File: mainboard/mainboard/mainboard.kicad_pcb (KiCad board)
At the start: 2 copper layers, 100 x 100 mm, 95 parts, among them IC501 SN74HCS138PWR, IC502 SN74HCS138PWR, IC503 SN74HCS138PWR, IC504 SN74HCS138PWR, IC505 SN74HCS151PWR, J201 Power LED connector, J202 Power button connector, J301 DC-005-5A-2.0, J601 Connector 1, J602 Connector 6, J603 Connector 5, J604 Connector 4, J605 Connector 1, J606 Connector 3, J607 Connector 2, J608 I2C 2, J609 Conn_01x03_Female, J610 Conn_01x03_Female, J611 I2C 1, J612 I2C 3, J801 Micro_SD_Card, U201 RP2040, U301 LD1117S50TR_SOT223, U303 BD9D321EFJ, U304 BD9D321EFJ, U401 W25Q128JVS, U701 hs8836a, Y201 ECS-120-8-36-CGN-TR

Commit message: motherboard designed
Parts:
- added TP301: TestPoint, TestPoint:TestPoint_Loop_D1.80mm_Drill1.0mm_Beaded, F.Cu at (45.0, 149.0)
- added TP302: TestPoint, TestPoint:TestPoint_Pad_D1.5mm, F.Cu at (47.0, 141.0)
- added TP303: TestPoint, TestPoint:TestPoint_Loop_D1.80mm_Drill1.0mm_Beaded, F.Cu at (120.0, 85.0)
- added TP304: TestPoint, TestPoint:TestPoint_Loop_D1.80mm_Drill1.0mm_Beaded, F.Cu at (103.0, 128.0)
- added TP305: TestPoint, TestPoint:TestPoint_Pad_D1.5mm, F.Cu at (120.4, 89.6)
- added TP306: TestPoint, TestPoint:TestPoint_Pad_D1.5mm, F.Cu at (99.0, 125.0)
- moved R801 1.20 mm to (70.2, 114.9)
- moved R802 1.13 mm to (70.2, 118.4)
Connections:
- net +3V3_BUS renamed +3V3
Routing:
- net /Connectors/BUS.D0: track 91.7 -> 173.7 mm
- net /Connectors/BUS.D1: track 92.6 -> 174.1 mm
- net /Connectors/BUS.SCLK: track 92.6 -> 174.1 mm
- net /Connectors/BUS.RWDS: track 92.2 -> 173.7 mm
- net /Connectors/BUS.D2: track 92.8 -> 142.0 mm
- net /Connectors/BUS.D3: track 93.0 -> 142.0 mm
- net /RP2040 Core/SDIO.D2: track 36.2 -> 55.4 mm
- net /RP2040 Core/SDIO.D3: track 37.0 -> 55.5 mm
- net /RP2040 Core/SDIO.CMD: track 38.2 -> 55.4 mm
- net /Connectors/BUS.D6: track 92.9 -> 108.7 mm
- net /Connectors/BUS.D7: track 93.0 -> 108.7 mm
- net /Connectors/BUS.D4: track 92.9 -> 108.6 mm
- net /Connectors/BUS.D5: track 93.1 -> 108.7 mm
- net /RP2040 Core/SDIO.D1: track 41.8 -> 55.5 mm
- net /Flash memory/FLASH.SD2: track 8.12 -> 20.2 mm
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
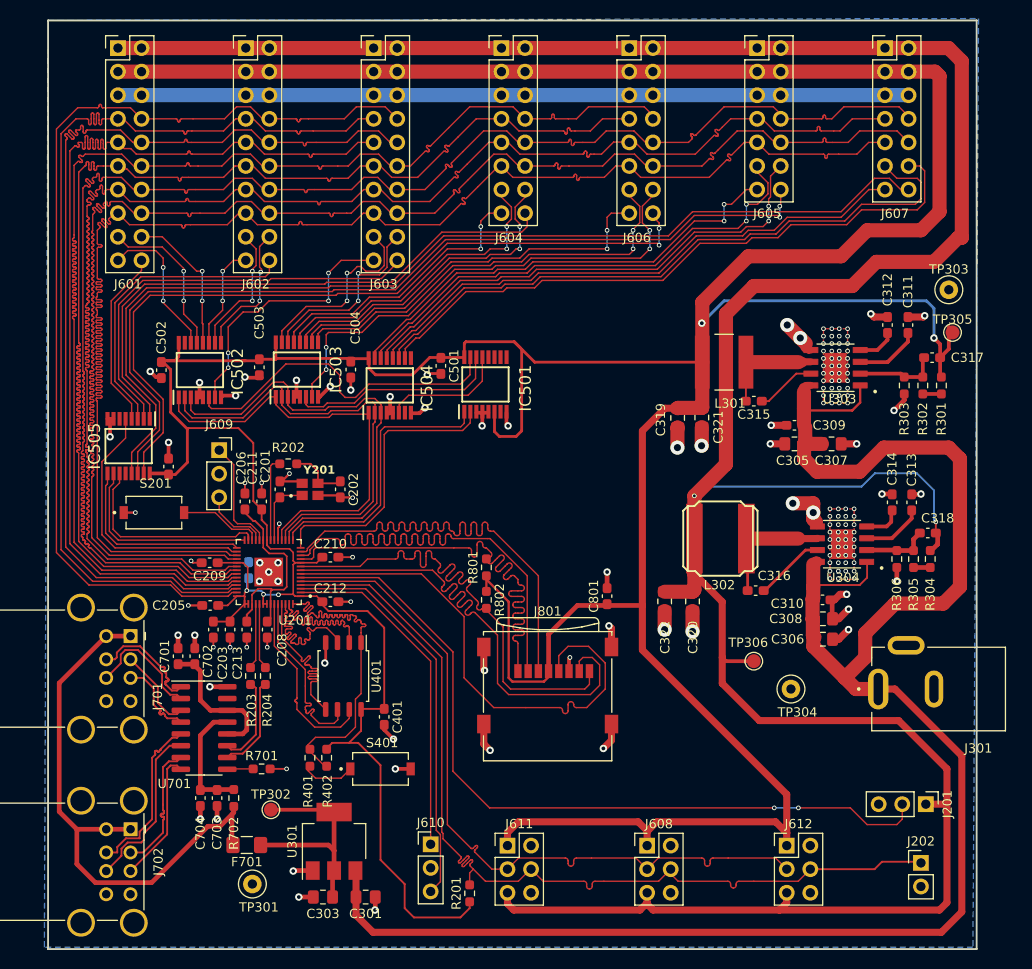
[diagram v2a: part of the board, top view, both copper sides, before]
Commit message: gpu and motherboard passes tests, now time for fpga
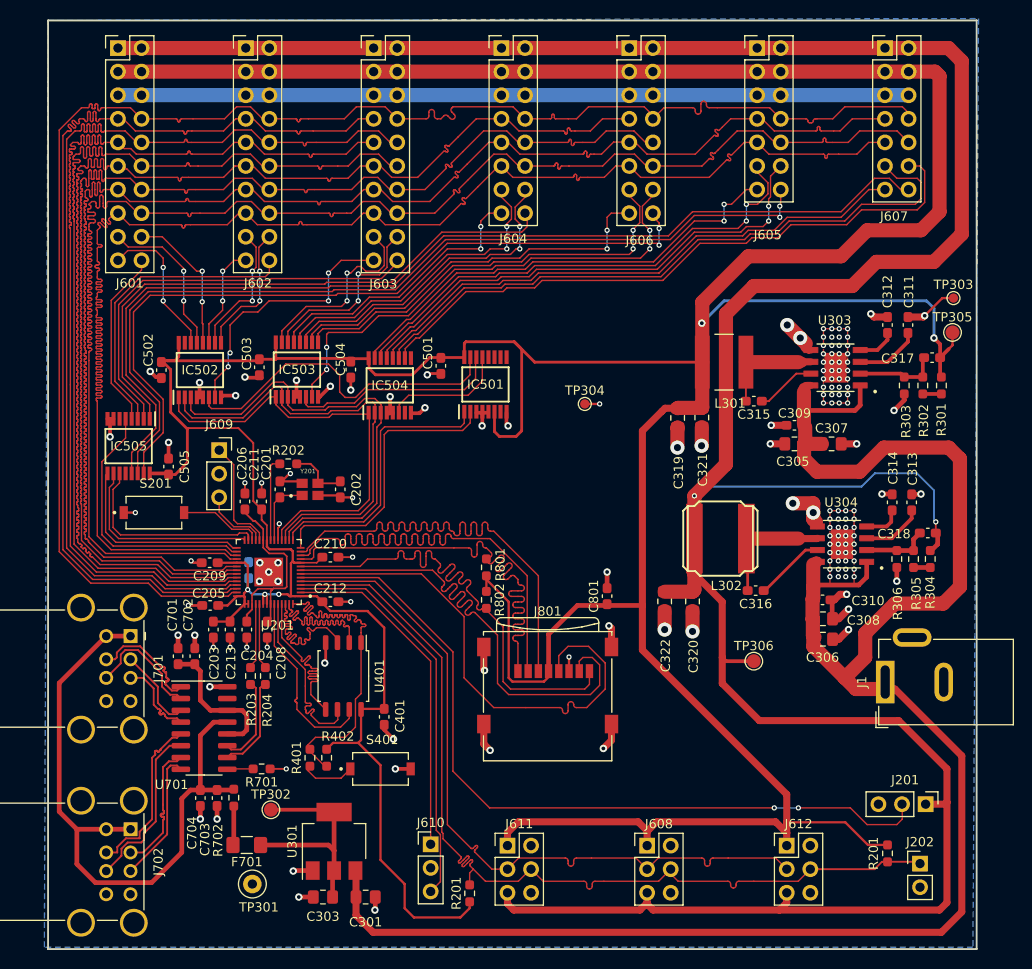
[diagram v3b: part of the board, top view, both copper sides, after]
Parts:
- removed J301: DC-005-5A-2.0, footprints:XKB_DC-005-5A-2.0
- added J1: Barrel_Jack_Switch, Connector_BarrelJack:BarrelJack_GCT_DCJ200-10-A_Horizontal, F.Cu at (113.2, 127.2)
- added R201: 10k, Resistor_SMD:R_0603_1608Metric_Pad0.98x0.95mm_HandSolder, F.Cu at (113.4, 145.7)
- TP303, TP304: footprint TestPoint:TestPoint_Loop_D1.80mm_Drill1.0mm_Beaded -> TestPoint:TestPoint_Pad_D1.0mm
- moved TP304 37.9 mm to (80.8, 97.3)
- moved TP303 1.03 mm to (120.5, 85.9)
- moved J202 0.13 mm to (116.9, 146.8)
- turned R702 to 90 degrees
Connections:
- net /Bus multiplexers & demultiplexers/BUS.CS0 renamed /Bus multiplexers & demultiplexers/BUS_CS0
- net /Bus multiplexers & demultiplexers/BUS.CS1 renamed /Bus multiplexers & demultiplexers/BUS_CS1
- net /Bus multiplexers & demultiplexers/BUS.CS10 renamed /Bus multiplexers & demultiplexers/BUS_CS10
- net /Bus multiplexers & demultiplexers/BUS.CS11 renamed /Bus multiplexers & demultiplexers/BUS_CS11
- net /Bus multiplexers & demultiplexers/BUS.CS12 renamed /Bus multiplexers & demultiplexers/BUS_CS12
- net /Bus multiplexers & demultiplexers/BUS.CS13 renamed /Bus multiplexers & demultiplexers/BUS_CS13
- net /Bus multiplexers & demultiplexers/BUS.CS2 renamed /Bus multiplexers & demultiplexers/BUS_CS2
- net /Bus multiplexers & demultiplexers/BUS.CS3 renamed /Bus multiplexers & demultiplexers/BUS_CS3
- net /Bus multiplexers & demultiplexers/BUS.CS4 renamed /Bus multiplexers & demultiplexers/BUS_CS4
- net /Bus multiplexers & demultiplexers/BUS.CS5 renamed /Bus multiplexers & demultiplexers/BUS_CS5
- net /Bus multiplexers & demultiplexers/BUS.CS6 renamed /Bus multiplexers & demultiplexers/BUS_CS6
- net /Bus multiplexers & demultiplexers/BUS.CS7 renamed /Bus multiplexers & demultiplexers/BUS_CS7
- net /Bus multiplexers & demultiplexers/BUS.CS8 renamed /Bus multiplexers & demultiplexers/BUS_CS8
- net /Bus multiplexers & demultiplexers/BUS.CS9 renamed /Bus multiplexers & demultiplexers/BUS_CS9
- net /Bus multiplexers & demultiplexers/BUS.CTRL0 renamed /Bus multiplexers & demultiplexers/BUS_CTRL0
- net /Bus multiplexers & demultiplexers/BUS.CTRL1 renamed /Bus multiplexers & demultiplexers/BUS_CTRL1
- net /Bus multiplexers & demultiplexers/BUS.CTRL2 renamed /Bus multiplexers & demultiplexers/BUS_CTRL2
- net /Bus multiplexers & demultiplexers/BUS.CTRL3 renamed /Bus multiplexers & demultiplexers/BUS_CTRL3
- net /Bus multiplexers & demultiplexers/BUS.CTRL4 renamed /Bus multiplexers & demultiplexers/BUS_CTRL4
- net /Bus multiplexers & demultiplexers/BUS.INT0 renamed /Bus multiplexers & demultiplexers/BUS_INT0
- net /Bus multiplexers & demultiplexers/BUS.INT1 renamed /Bus multiplexers & demultiplexers/BUS_INT1
- net /Bus multiplexers & demultiplexers/BUS.INT2 renamed /Bus multiplexers & demultiplexers/BUS_INT2
- net /Bus multiplexers & demultiplexers/BUS.INT3 renamed /Bus multiplexers & demultiplexers/BUS_INT3
- net /Bus multiplexers & demultiplexers/BUS.INT4 renamed /Bus multiplexers & demultiplexers/BUS_INT4
- net /Bus multiplexers & demultiplexers/BUS.INT5 renamed /Bus multiplexers & demultiplexers/BUS_INT5
- net /Bus multiplexers & demultiplexers/BUS.INT6 renamed /Bus multiplexers & demultiplexers/BUS_INT6
- net /Bus multiplexers & demultiplexers/BUS.RE0 renamed /Bus multiplexers & demultiplexers/BUS_RE0
- net /Bus multiplexers & demultiplexers/BUS.RE1 renamed /Bus multiplexers & demultiplexers/BUS_RE1
- net /Bus multiplexers & demultiplexers/BUS.RE2 renamed /Bus multiplexers & demultiplexers/BUS_RE2
- net /Bus multiplexers & demultiplexers/BUS.RE3 renamed /Bus multiplexers & demultiplexers/BUS_RE3
- net /Bus multiplexers & demultiplexers/BUS.RE4 renamed /Bus multiplexers & demultiplexers/BUS_RE4
- net /Bus multiplexers & demultiplexers/BUS.RE5 renamed /Bus multiplexers & demultiplexers/BUS_RE5
- net /Bus multiplexers & demultiplexers/BUS.RE6 renamed /Bus multiplexers & demultiplexers/BUS_RE6
- net DEMUX_1_EN renamed /Bus multiplexers & demultiplexers/DEMUX_1_EN
- net DEMUX_2_EN renamed /Bus multiplexers & demultiplexers/DEMUX_2_EN
- net DEMUX_3_EN renamed /Bus multiplexers & demultiplexers/DEMUX_3_EN
- net OSC_XIN renamed /RP2040 Core/OSC_IN
- net OSC_XOUT renamed /RP2040 Core/OSC_OUT
- net POWER_LED renamed /Connectors/POWER_LED
- C703 pad 1: Net-(U701-VCC) -> +5V_USB_HUB
- C704 pad 1: Net-(U701-VCC) -> +5V_USB_HUB
- F701 pad 2: +5V_USB_HUB -> Net-(F701-Pad2)
- IC501 pad 12: /Bus multiplexers & demultiplexers/BUS.RE_USB -> unconnected-(IC501-Y3)
- IC504 pad 7: /Bus multiplexers & demultiplexers/BUS.RE7 -> unconnected-(IC504-Y7)
- IC504 pad 9: /Bus multiplexers & demultiplexers/BUS.CS14 -> unconnected-(IC504-Y6)
- IC505 pad 12: /Bus multiplexers & demultiplexers/BUS.INT7 -> unconnected-(IC505-D7)
- J601 pad 10: /Connectors/BUS.D5 -> /Connectors/BUS.D6
- J601 pad 11: /Connectors/BUS.D2 -> /Connectors/BUS.D3
- J601 pad 12: /Connectors/BUS.D3 -> /Connectors/BUS.D4
- J601 pad 13: /Connectors/BUS.D0 -> /Connectors/BUS.D1
- J601 pad 14: /Connectors/BUS.D1 -> /Connectors/BUS.D2
- J601 pad 16: /Connectors/BUS.RWDS -> /Connectors/BUS.D0
- J601 pad 7: /Connectors/BUS.D6 -> /Connectors/BUS.D7
- J601 pad 8: /Connectors/BUS.D7 -> /Connectors/BUS.RWDS
- J601 pad 9: /Connectors/BUS.D4 -> /Connectors/BUS.D5
- J602 pad 10: /Connectors/BUS.D5 -> /Connectors/BUS.D6
- J602 pad 11: /Connectors/BUS.D2 -> /Connectors/BUS.D3
- J602 pad 12: /Connectors/BUS.D3 -> /Connectors/BUS.D4
- J602 pad 13: /Connectors/BUS.D0 -> /Connectors/BUS.D1
- J602 pad 14: /Connectors/BUS.D1 -> /Connectors/BUS.D2
- J602 pad 16: /Connectors/BUS.RWDS -> /Connectors/BUS.D0
- J602 pad 7: /Connectors/BUS.D6 -> /Connectors/BUS.D7
- J602 pad 8: /Connectors/BUS.D7 -> /Connectors/BUS.RWDS
- J602 pad 9: /Connectors/BUS.D4 -> /Connectors/BUS.D5
- J603 pad 10: /Connectors/BUS.D5 -> /Connectors/BUS.D6
- J603 pad 11: /Connectors/BUS.D2 -> /Connectors/BUS.D3
- J603 pad 12: /Connectors/BUS.D3 -> /Connectors/BUS.D4
- J603 pad 13: /Connectors/BUS.D0 -> /Connectors/BUS.D1
- J603 pad 14: /Connectors/BUS.D1 -> /Connectors/BUS.D2
- J603 pad 16: /Connectors/BUS.RWDS -> /Connectors/BUS.D0
- J603 pad 7: /Connectors/BUS.D6 -> /Connectors/BUS.D7
- J603 pad 8: /Connectors/BUS.D7 -> /Connectors/BUS.RWDS
- J603 pad 9: /Connectors/BUS.D4 -> /Connectors/BUS.D5
- J604 pad 10: /Connectors/BUS.D1 -> /Connectors/BUS.D2
- J604 pad 12: /Connectors/BUS.RWDS -> /Connectors/BUS.D0
- J604 pad 7: /Connectors/BUS.D2 -> /Connectors/BUS.D3
- J604 pad 8: /Connectors/BUS.D3 -> /Connectors/BUS.RWDS
- J604 pad 9: /Connectors/BUS.D0 -> /Connectors/BUS.D1
- J605 pad 10: /Connectors/BUS.RWDS -> /Connectors/BUS.D0
- J605 pad 7: /Connectors/BUS.D0 -> /Connectors/BUS.D1
- J605 pad 8: /Connectors/BUS.D1 -> /Connectors/BUS.RWDS
- J606 pad 10: /Connectors/BUS.D1 -> /Connectors/BUS.D2
- J606 pad 12: /Connectors/BUS.RWDS -> /Connectors/BUS.D0
- J606 pad 7: /Connectors/BUS.D2 -> /Connectors/BUS.D3
- J606 pad 8: /Connectors/BUS.D3 -> /Connectors/BUS.RWDS
- J606 pad 9: /Connectors/BUS.D0 -> /Connectors/BUS.D1
- J607 pad 10: /Connectors/BUS.RWDS -> /Connectors/BUS.D0
- J607 pad 7: /Connectors/BUS.D0 -> /Connectors/BUS.D1
- J607 pad 8: /Connectors/BUS.D1 -> /Connectors/BUS.RWDS
- R702 pad 1: Net-(U701-VCC) -> Net-(F701-Pad2)
- TP304 pad 1: (no net) -> GND
- U201 pad 32: /Connectors/BUS.RWDS -> /Connectors/BUS.D0
- U201 pad 34: /Connectors/BUS.D0 -> /Connectors/BUS.D1
- U201 pad 35: /Connectors/BUS.D1 -> /Connectors/BUS.D2
- U201 pad 36: /Connectors/BUS.D2 -> /Connectors/BUS.D3
- U201 pad 37: /Connectors/BUS.D3 -> /Connectors/BUS.D4
- U201 pad 38: /Connectors/BUS.D4 -> /Connectors/BUS.D5
- U201 pad 39: /Connectors/BUS.D5 -> /Connectors/BUS.D6
- U201 pad 40: /Connectors/BUS.D6 -> /Connectors/BUS.D7
- U201 pad 41: /Connectors/BUS.D7 -> /Connectors/BUS.RWDS
- U701 pad 13: Net-(U701-VCC) -> +5V_USB_HUB
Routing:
- net Net-(U701-VCC): track 13.0 -> 0.00 mm
- net +3V3: track 526.9 -> 539.0 mm
- net +5V_USB_HUB: track 60.9 -> 70.5 mm
- net GND: track 216.8 -> 223.8 mm, vias 155 -> 148
- net Net-(F701-Pad2): track 0.00 -> 4.22 mm
- net /Connectors/BUS.RWDS: track 173.7 -> 175.8 mm
- net /Connectors/BUS.D6: track 108.7 -> 109.9 mm
- net /Connectors/BUS.D0: track 173.7 -> 174.9 mm
- net /Connectors/BUS.SCLK: track 174.1 -> 174.9 mm
- net /Connectors/BUS.D4: track 108.6 -> 109.3 mm
- net /Connectors/BUS.D1: track 174.1 -> 174.9 mm
- net /Connectors/BUS.D7: track 108.7 -> 109.3 mm
- net /Connectors/BUS.D5: track 108.7 -> 109.2 mm
- net /Connectors/BUS.D2: track 142.0 -> 142.5 mm
- net /Connectors/BUS.D3: track 142.0 -> 142.5 mm

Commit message: refactored mainboard schematic
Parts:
- IC501: value SN74HCS138PWR -> SN74HCS238PWR
- moved J604 1.22 mm to (71.9, 60.2)
- moved J605 1.22 mm to (99.5, 60.2)
- moved J606 1.22 mm to (85.7, 60.2)
- moved J607 1.22 mm to (113.2, 60.2)
- moved J601 1.22 mm to (30.6, 60.2)
- moved J602 1.22 mm to (44.4, 60.2)
- moved J603 1.22 mm to (58.2, 60.2)
- moved IC501 0.10 mm to (70.1, 95.3)
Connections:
- J601 pad 2: +5V_BUS -> VDC
- J602 pad 2: +5V_BUS -> VDC
- J603 pad 2: +5V_BUS -> VDC
- J604 pad 2: +5V_BUS -> VDC
- J605 pad 2: +5V_BUS -> VDC
- J606 pad 2: +5V_BUS -> VDC
- J607 pad 2: +5V_BUS -> VDC
- J608 pad 2: unconnected-(J608-Pin_2) -> VDC
- J611 pad 2: unconnected-(J611-Pin_2) -> VDC
- J612 pad 2: unconnected-(J612-Pin_2) -> VDC
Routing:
- net VDC: track 196.5 -> 393.8 mm, vias 0 -> 4
- net +5V_BUS: track 322.6 -> 345.1 mm
- net /Bus multiplexers & demultiplexers/BUS_CS4: track 28.6 -> 26.2 mm
- net /Bus multiplexers & demultiplexers/BUS_RE2: track 20.3 -> 18.4 mm
- net /Bus multiplexers & demultiplexers/BUS_CS3: track 14.5 -> 12.7 mm
- net /Connectors/BUS.D3: track 142.5 -> 144.3 mm
- net /Bus multiplexers & demultiplexers/BUS_RE1: track 14.6 -> 12.9 mm
- net /Bus multiplexers & demultiplexers/BUS_INT3: track 62.0 -> 60.4 mm
- net /Bus multiplexers & demultiplexers/BUS_INT2: track 45.6 -> 44.0 mm
- net /Bus multiplexers & demultiplexers/BUS_INT1: track 32.8 -> 31.2 mm
- net /Connectors/BUS.D1: track 174.9 -> 176.4 mm
- net /Connectors/BUS.D4: track 109.3 -> 110.8 mm
- net /Connectors/BUS.D5: track 109.2 -> 110.7 mm
- net /Bus multiplexers & demultiplexers/BUS_INT6: track 110.8 -> 109.4 mm
- net +3V3: track 539.0 -> 537.6 mm
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
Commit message: working on new pcb
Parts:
- removed C201, C202: 14p, Capacitor_SMD:C_0603_1608Metric_Pad1.08x0.95mm_HandSolder
- removed C204, C311, C313: 1u, Capacitor_SMD:C_0603_1608Metric_Pad1.08x0.95mm_HandSolder
- removed C206, C208, C209, C210, C211, C212, C213, C309, C310, C315, C316, C401, C501, C502, C503, C504, C505, C702, C704: 100n, Capacitor_SMD:C_0603_1608Metric_Pad1.08x0.95mm_HandSolder
- removed C301: 4.7u, Capacitor_SMD:C_0805_2012Metric_Pad1.18x1.45mm_HandSolder
- removed C303: 10uF, Capacitor_SMD:C_0805_2012Metric_Pad1.18x1.45mm_HandSolder
- removed C305, C306, C307, C308: 10u, Capacitor_SMD:C_0805_2012Metric_Pad1.18x1.45mm_HandSolder
- removed C312, C314: 3300p, Capacitor_SMD:C_0603_1608Metric_Pad1.08x0.95mm_HandSolder
- removed C317, C318: 22p, Capacitor_SMD:C_0603_1608Metric_Pad1.08x0.95mm_HandSolder
- removed C319, C320, C321, C322: 22u, Capacitor_SMD:C_0805_2012Metric_Pad1.18x1.45mm_HandSolder
- removed C701, C703: 4.7u, Capacitor_SMD:C_0603_1608Metric_Pad1.08x0.95mm_HandSolder
- removed C801: 10u, Capacitor_SMD:C_0603_1608Metric_Pad1.08x0.95mm_HandSolder
- removed F701: 500mA, Fuse:Fuse_1206_3216Metric_Pad1.42x1.75mm_HandSolder
- removed IC501: SN74HCS238PWR, footprints:SOP65P640X120-16N
- removed IC502, IC503, IC504: SN74HCS138PWR, footprints:SOP65P640X120-16N
- removed IC505: SN74HCS151PWR, footprints:SOP65P640X120-16N
- removed J201: Power LED connector, Connector_PinHeader_2.54mm:PinHeader_1x03_P2.54mm_Vertical
- removed J202: Power button connector, Connector_PinHeader_2.54mm:PinHeader_1x02_P2.54mm_Vertical
- removed J601: Connector 1, Connector_PinHeader_2.54mm:PinHeader_2x10_P2.54mm_Vertical
- removed J602: Connector 6, Connector_PinHeader_2.54mm:PinHeader_2x10_P2.54mm_Vertical
- removed J603: Connector 5, Connector_PinHeader_2.54mm:PinHeader_2x10_P2.54mm_Vertical
- removed J604: Connector 4, Connector_PinHeader_2.54mm:PinHeader_2x08_P2.54mm_Vertical
- removed J605: Connector 1, Connector_PinHeader_2.54mm:PinHeader_2x07_P2.54mm_Vertical
- removed J606: Connector 3, Connector_PinHeader_2.54mm:PinHeader_2x08_P2.54mm_Vertical
- removed J607: Connector 2, Connector_PinHeader_2.54mm:PinHeader_2x07_P2.54mm_Vertical
- removed J608: I2C 2, Connector_PinHeader_2.54mm:PinHeader_2x03_P2.54mm_Vertical
- removed J609: Conn_01x03_Female, Connector_PinSocket_2.54mm:PinSocket_1x03_P2.54mm_Vertical
- removed J610: Conn_01x03_Female, Connector_PinHeader_2.54mm:PinHeader_1x03_P2.54mm_Vertical
- removed J611: I2C 1, Connector_PinHeader_2.54mm:PinHeader_2x03_P2.54mm_Vertical
- removed J612: I2C 3, Connector_PinHeader_2.54mm:PinHeader_2x03_P2.54mm_Vertical
- removed J701, J702: ~, Connector_USB:USB_A_Wuerth_61400826021_Horizontal_Stacked
- removed J801: Micro_SD_Card, Connector_Card:microSD_HC_Wuerth_693072010801
- removed L301: 2.2u, footprints:IND_NR6028T4R7M
- removed L302: 3.3u, footprints:NRS8030
- removed R201 (x2), R402, R801, R802: 10k, Resistor_SMD:R_0603_1608Metric_Pad0.98x0.95mm_HandSolder
- removed R202, R401: 1k, Resistor_SMD:R_0603_1608Metric_Pad0.98x0.95mm_HandSolder
- removed R203, R204: 27.4R, Resistor_SMD:R_0603_1608Metric_Pad0.98x0.95mm_HandSolder
- removed R301: 68k, Resistor_SMD:R_0603_1608Metric_Pad0.98x0.95mm_HandSolder
- removed R302: 5.6k, Resistor_SMD:R_0603_1608Metric_Pad0.98x0.95mm_HandSolder
- removed R303, R306: 22k, Resistor_SMD:R_0603_1608Metric_Pad0.98x0.95mm_HandSolder
- removed R304: 120k, Resistor_SMD:R_0603_1608Metric_Pad0.98x0.95mm_HandSolder
- removed R305: 3.3k, Resistor_SMD:R_0603_1608Metric_Pad0.98x0.95mm_HandSolder
- removed R701: 100k, Resistor_SMD:R_0603_1608Metric_Pad0.98x0.95mm_HandSolder
- removed R702: 4.7, Resistor_SMD:R_0603_1608Metric_Pad0.98x0.95mm_HandSolder
- removed S201, S401: PTS636_SM43J_SMTR_LFS, footprints:SW_PTS636_SM43J_SMTR_LFS
- removed TP301: TestPoint, TestPoint:TestPoint_Loop_D1.80mm_Drill1.0mm_Beaded
- removed TP302, TP305, TP306: TestPoint, TestPoint:TestPoint_Pad_D1.5mm
- removed TP303, TP304: TestPoint, TestPoint:TestPoint_Pad_D1.0mm
- removed U201: RP2040, footprints:QFN40P700X700X90-57N
- removed U301: LD1117S50TR_SOT223, Package_TO_SOT_SMD:SOT-223-3_TabPin2
- removed U303, U304: BD9D321EFJ, footprints:SOIC127P600X100-9N
- removed U401: W25Q128JVS, Package_SO:SOIC-8_5.23x5.23mm_P1.27mm
- removed U701: hs8836a, Package_SO:SOP-16_3.9x9.9mm_P1.27mm
- removed Y201: ECS-120-8-36-CGN-TR, footprints:XTAL_ECS-120-8-36-CGN-TR
- added C1: 14p, Capacitor_SMD:C_0402_1005Metric_Pad0.74x0.62mm_HandSolder, F.Cu at (65.2, 57.8)
- added C10: 100n, Capacitor_SMD:C_0402_1005Metric_Pad0.74x0.62mm_HandSolder, F.Cu at (68.7, 63.8)
- added C11: 100n, Capacitor_SMD:C_0402_1005Metric_Pad0.74x0.62mm_HandSolder, F.Cu at (66.7, 69.1)
- added C12: 100n, Capacitor_SMD:C_0402_1005Metric_Pad0.74x0.62mm_HandSolder, F.Cu at (62.1, 71.9)
- added C13: 100n, Capacitor_SMD:C_0402_1005Metric_Pad0.74x0.62mm_HandSolder, F.Cu at (56.3, 69.2)
- added C14: 100n, Capacitor_SMD:C_0402_1005Metric_Pad0.74x0.62mm_HandSolder, F.Cu at (61.0, 71.2)
- added C15: 1u, Capacitor_SMD:C_0402_1005Metric_Pad0.74x0.62mm_HandSolder, F.Cu at (245.2, 61.9)
- added C16: 1u, Capacitor_SMD:C_0402_1005Metric_Pad0.74x0.62mm_HandSolder, F.Cu at (254.8, 63.9)
- added C17: 4.7u, Capacitor_SMD:C_0402_1005Metric_Pad0.74x0.62mm_HandSolder, F.Cu at (245.2, 60.0)
- added C18: 100pF, Capacitor_SMD:C_0402_1005Metric_Pad0.74x0.62mm_HandSolder, F.Cu at (245.2, 65.9)
- added C19: 100pF, Capacitor_SMD:C_0402_1005Metric_Pad0.74x0.62mm_HandSolder, F.Cu at (254.8, 65.9)
- added C2: 14p, Capacitor_SMD:C_0402_1005Metric_Pad0.74x0.62mm_HandSolder, F.Cu at (62.3, 54.4)
- added C20: 10uF, Capacitor_SMD:C_0402_1005Metric_Pad0.74x0.62mm_HandSolder, F.Cu at (245.2, 63.9)
- added C21: 2.2u, Capacitor_SMD:C_0402_1005Metric_Pad0.74x0.62mm_HandSolder, F.Cu at (254.8, 61.9)
- added C22: 2.2u, Capacitor_SMD:C_0402_1005Metric_Pad0.74x0.62mm_HandSolder, F.Cu at (254.8, 67.9)
- added C23: 10u, Capacitor_SMD:C_1206_3216Metric_Pad1.33x1.80mm_HandSolder, F.Cu at (134.1, 108.7)
- added C24: 10u, Capacitor_SMD:C_1206_3216Metric_Pad1.33x1.80mm_HandSolder, F.Cu at (117.0, 108.5)
- added C25: 10u, Capacitor_SMD:C_1206_3216Metric_Pad1.33x1.80mm_HandSolder, F.Cu at (131.4, 108.7)
- added C26: 10u, Capacitor_SMD:C_1206_3216Metric_Pad1.33x1.80mm_HandSolder, F.Cu at (114.3, 108.5)
- added C27: 100n, Capacitor_SMD:C_0402_1005Metric_Pad0.74x0.62mm_HandSolder, F.Cu at (136.0, 108.1)
- added C28: 100n, Capacitor_SMD:C_0402_1005Metric_Pad0.74x0.62mm_HandSolder, F.Cu at (118.9, 107.8)
- added C29: 1u, Capacitor_SMD:C_0402_1005Metric_Pad0.74x0.62mm_HandSolder, F.Cu at (144.3, 115.3)
- added C3: 1u, Capacitor_SMD:C_0402_1005Metric_Pad0.74x0.62mm_HandSolder, F.Cu at (58.7, 71.2)
- added C30: 3300p, Capacitor_SMD:C_0402_1005Metric_Pad0.74x0.62mm_HandSolder, F.Cu at (144.3, 114.2)
- added C31: 1u, Capacitor_SMD:C_0402_1005Metric_Pad0.74x0.62mm_HandSolder, F.Cu at (126.9, 115.2)
- added C32: 3300p, Capacitor_SMD:C_0402_1005Metric_Pad0.74x0.62mm_HandSolder, F.Cu at (126.9, 114.1)
- added C33: 100n, Capacitor_SMD:C_0402_1005Metric_Pad0.74x0.62mm_HandSolder, F.Cu at (135.0, 101.9)
- added C34: 100n, Capacitor_SMD:C_0402_1005Metric_Pad0.74x0.62mm_HandSolder, F.Cu at (119.5, 102.5)
- added C35: 22p, Capacitor_SMD:C_0402_1005Metric_Pad0.74x0.62mm_HandSolder, F.Cu at (140.3, 116.5)
- added C36: 22p, Capacitor_SMD:C_0402_1005Metric_Pad0.74x0.62mm_HandSolder, F.Cu at (123.2, 116.3)
- added C37: 22u, Capacitor_SMD:C_1206_3216Metric_Pad1.33x1.80mm_HandSolder, F.Cu at (144.7, 93.6)
- added C38: 22u, Capacitor_SMD:C_1206_3216Metric_Pad1.33x1.80mm_HandSolder, F.Cu at (127.6, 95.2)
- added C39: 22u, Capacitor_SMD:C_1206_3216Metric_Pad1.33x1.80mm_HandSolder, F.Cu at (144.7, 90.9)
- added C4: 100n, Capacitor_SMD:C_0402_1005Metric_Pad0.74x0.62mm_HandSolder, F.Cu at (57.5, 71.2)
- added C40: 22u, Capacitor_SMD:C_1206_3216Metric_Pad1.33x1.80mm_HandSolder, F.Cu at (127.6, 92.6)
- added C41: 4.7u, Capacitor_SMD:C_0402_1005Metric_Pad0.74x0.62mm_HandSolder, F.Cu at (40.0, 121.1)
- added C42: 100n, Capacitor_SMD:C_0402_1005Metric_Pad0.74x0.62mm_HandSolder, F.Cu at (40.0, 123.0)
- added C43: 4.7u, Capacitor_SMD:C_0402_1005Metric_Pad0.74x0.62mm_HandSolder, F.Cu at (40.0, 125.0)
- added C44: 1u, Capacitor_SMD:C_0402_1005Metric_Pad0.74x0.62mm_HandSolder, F.Cu at (60.6, 107.5)
- added C45: 100n, Capacitor_SMD:C_0402_1005Metric_Pad0.74x0.62mm_HandSolder, F.Cu at (70.0, 100.3)
- added C46: 100n, Capacitor_SMD:C_0402_1005Metric_Pad0.74x0.62mm_HandSolder, F.Cu at (69.3, 104.8)
- added C47: 1u, Capacitor_SMD:C_0402_1005Metric_Pad0.74x0.62mm_HandSolder, F.Cu at (61.8, 107.5)
- added C48: 100n, Capacitor_SMD:C_0402_1005Metric_Pad0.74x0.62mm_HandSolder, F.Cu at (58.3, 104.7)
- added C49: 100n, Capacitor_SMD:C_0402_1005Metric_Pad0.74x0.62mm_HandSolder, F.Cu at (66.6, 108.5)
- added C5: 1u, Capacitor_SMD:C_0402_1005Metric_Pad0.74x0.62mm_HandSolder, F.Cu at (59.8, 71.2)
- added C50: 100n, Capacitor_SMD:C_0402_1005Metric_Pad0.74x0.62mm_HandSolder, F.Cu at (65.4, 108.5)
- added C51: 100n, Capacitor_SMD:C_0402_1005Metric_Pad0.74x0.62mm_HandSolder, F.Cu at (62.9, 94.0)
- added C52: 100n, Capacitor_SMD:C_0402_1005Metric_Pad0.74x0.62mm_HandSolder, F.Cu at (63.8, 107.8)
- added C53: 100n, Capacitor_SMD:C_0402_1005Metric_Pad0.74x0.62mm_HandSolder, F.Cu at (64.0, 94.0)
- added C54: 100n, Capacitor_SMD:C_0402_1005Metric_Pad0.74x0.62mm_HandSolder, F.Cu at (58.0, 100.0)
- added C55: 100n, Capacitor_SMD:C_0402_1005Metric_Pad0.74x0.62mm_HandSolder, F.Cu at (59.5, 107.5)
- added C56: 1u, Capacitor_SMD:C_0402_1005Metric_Pad0.74x0.62mm_HandSolder, F.Cu at (232.8, 103.5)
- added C57: 1u, Capacitor_SMD:C_0402_1005Metric_Pad0.74x0.62mm_HandSolder, F.Cu at (232.8, 97.6)
- added C58: 1u, Capacitor_SMD:C_0402_1005Metric_Pad0.74x0.62mm_HandSolder, F.Cu at (236.0, 95.6)
- added C59: 1u, Capacitor_SMD:C_0402_1005Metric_Pad0.74x0.62mm_HandSolder, F.Cu at (239.3, 97.6)
- added C6: 100n, Capacitor_SMD:C_0402_1005Metric_Pad0.74x0.62mm_HandSolder, F.Cu at (61.7, 57.7)
- added C60: 1u, Capacitor_SMD:C_0402_1005Metric_Pad0.74x0.62mm_HandSolder, F.Cu at (232.8, 101.5)
- added C61: 100n, Capacitor_SMD:C_0402_1005Metric_Pad0.74x0.62mm_HandSolder, F.Cu at (239.3, 99.6)
- added C62: 100n, Capacitor_SMD:C_0402_1005Metric_Pad0.74x0.62mm_HandSolder, F.Cu at (232.8, 95.6)
- added C63: 100n, Capacitor_SMD:C_0402_1005Metric_Pad0.74x0.62mm_HandSolder, F.Cu at (232.8, 99.6)
- added C64: 22u, Capacitor_SMD:C_0402_1005Metric_Pad0.74x0.62mm_HandSolder, F.Cu at (236.0, 103.5)
- added C65: 100n, Capacitor_SMD:C_0402_1005Metric_Pad0.74x0.62mm_HandSolder, F.Cu at (239.3, 95.6)
- added C66: 1u, Capacitor_SMD:C_0402_1005Metric_Pad0.74x0.62mm_HandSolder, F.Cu at (236.0, 97.6)
- added C67: 1u, Capacitor_SMD:C_0402_1005Metric_Pad0.74x0.62mm_HandSolder, F.Cu at (236.0, 99.6)
- added C68: 1u, Capacitor_SMD:C_0402_1005Metric_Pad0.74x0.62mm_HandSolder, F.Cu at (236.0, 101.5)
- added C69: 100n, Capacitor_SMD:C_0402_1005Metric_Pad0.74x0.62mm_HandSolder, F.Cu at (110.2, 97.4)
- added C7: 100n, Capacitor_SMD:C_0402_1005Metric_Pad0.74x0.62mm_HandSolder, F.Cu at (63.2, 72.5)
- added C70: 100n, Capacitor_SMD:C_0402_1005Metric_Pad0.74x0.62mm_HandSolder, F.Cu at (102.5, 98.7)
- added C71: 100n, Capacitor_SMD:C_0402_1005Metric_Pad0.74x0.62mm_HandSolder, F.Cu at (87.5, 92.2)
- added C72: 10u, Capacitor_SMD:C_0402_1005Metric_Pad0.74x0.62mm_HandSolder, F.Cu at (306.6, 64.0)
- added C72: 4.7u, Capacitor_SMD:C_0402_1005Metric_Pad0.74x0.62mm_HandSolder, F.Cu at (249.1, 43.9)
- added C73: 14p, Capacitor_SMD:C_0402_1005Metric_Pad0.74x0.62mm_HandSolder, F.Cu at (70.4, 92.8)
- added C73: 100n, Capacitor_SMD:C_0402_1005Metric_Pad0.74x0.62mm_HandSolder, F.Cu at (249.1, 45.8)
- added C74: 4.7u, Capacitor_SMD:C_0402_1005Metric_Pad0.74x0.62mm_HandSolder, F.Cu at (249.1, 47.8)
- added C74: 14p, Capacitor_SMD:C_0402_1005Metric_Pad0.74x0.62mm_HandSolder, F.Cu at (68.2, 90.5)
- added C75: 100n, Capacitor_SMD:C_0402_1005Metric_Pad0.74x0.62mm_HandSolder, F.Cu at (76.8, 113.0)
- added C76: 100n, Capacitor_SMD:C_0402_1005Metric_Pad0.74x0.62mm_HandSolder, F.Cu at (61.1, 81.4)
- added C77: 100n, Capacitor_SMD:C_0402_1005Metric_Pad0.74x0.62mm_HandSolder, F.Cu at (82.3, 77.7)
- added C78: 100n, Capacitor_SMD:C_0402_1005Metric_Pad0.74x0.62mm_HandSolder, F.Cu at (85.7, 85.5)
- added C8: 100n, Capacitor_SMD:C_0402_1005Metric_Pad0.74x0.62mm_HandSolder, F.Cu at (55.6, 63.8)
- added C9: 100n, Capacitor_SMD:C_0402_1005Metric_Pad0.74x0.62mm_HandSolder, F.Cu at (60.6, 57.7)
- added D1: LESD5D5.0CT1G, footprints:TVS_LESD5D5.0CT1G, F.Cu at (24.3, 121.2)
- added D10: LESD5D5.0CT1G, footprints:TVS_LESD5D5.0CT1G, F.Cu at (81.5, 131.1)
- added D10: LESD5D5.0CT1G, footprints:TVS_LESD5D5.0CT1G, F.Cu at (28.2, 128.3)
- added D11: LESD5D5.0CT1G, footprints:TVS_LESD5D5.0CT1G, F.Cu at (63.0, 123.4)
- added D11: WS2812B, LED_SMD:LED_WS2812B_PLCC4_5.0x5.0mm_P3.2mm, F.Cu at (298.4, 90.5)
- added D2: LESD5D5.0CT1G, footprints:TVS_LESD5D5.0CT1G, F.Cu at (59.1, 116.4)
- added D2: LESD5D5.0CT1G, footprints:TVS_LESD5D5.0CT1G, F.Cu at (24.3, 123.6)
- added D3: LESD5D5.0CT1G, footprints:TVS_LESD5D5.0CT1G, F.Cu at (83.1, 131.1)
- added D3: LESD5D5.0CT1G, footprints:TVS_LESD5D5.0CT1G, F.Cu at (24.3, 126.0)
- added D4: LESD5D5.0CT1G, footprints:TVS_LESD5D5.0CT1G, F.Cu at (59.1, 118.7)
- added D4: LESD5D5.0CT1G, footprints:TVS_LESD5D5.0CT1G, F.Cu at (24.3, 128.3)
- added D5: LESD5D5.0CT1G, footprints:TVS_LESD5D5.0CT1G, F.Cu at (24.3, 130.7)
- added D5: LESD5D5.0CT1G, footprints:TVS_LESD5D5.0CT1G, F.Cu at (63.0, 116.4)
- added D6: LESD5D5.0CT1G, footprints:TVS_LESD5D5.0CT1G, F.Cu at (24.3, 133.0)
- added D6: LESD5D5.0CT1G, footprints:TVS_LESD5D5.0CT1G, F.Cu at (59.1, 121.1)
- added D7: LESD5D5.0CT1G, footprints:TVS_LESD5D5.0CT1G, F.Cu at (28.2, 121.2)
- added D7: LESD5D5.0CT1G, footprints:TVS_LESD5D5.0CT1G, F.Cu at (63.0, 118.7)
- added D8: LESD5D5.0CT1G, footprints:TVS_LESD5D5.0CT1G, F.Cu at (59.1, 123.4)
- added D8: LESD5D5.0CT1G, footprints:TVS_LESD5D5.0CT1G, F.Cu at (28.2, 123.6)
- added D9: LESD5D5.0CT1G, footprints:TVS_LESD5D5.0CT1G, F.Cu at (28.2, 126.0)
- added D9: LESD5D5.0CT1G, footprints:TVS_LESD5D5.0CT1G, F.Cu at (63.0, 121.1)
- added IC1: SN74HCS151PWR, footprints:SOP65P640X120-16N, F.Cu at (99.1, 94.6)
- added IC2: SN74HCS151PWR, footprints:SOP65P640X120-16N, F.Cu at (106.7, 94.6)
- added IC3: SN74HCS138PWR, footprints:SOP65P640X120-16N, F.Cu at (91.4, 94.6)
- added IC4: SN74HCS138PWR, footprints:SOP65P640X120-16N, F.Cu at (80.0, 81.3)
- added IC5: SN74HCS138PWR, footprints:SOP65P640X120-16N, F.Cu at (80.0, 87.6)
- added J10: AudioJack4, Connector_Audio:Jack_3.5mm_PJ320D_Horizontal, F.Cu at (103.0, 126.4)
- added J11: AudioJack4, Connector_Audio:Jack_3.5mm_PJ320D_Horizontal, F.Cu at (115.4, 126.4)
- added J12: Conn_01x03_Female, Connector_PinHeader_2.54mm:PinHeader_1x03_P2.54mm_Vertical, F.Cu at (54.4, 54.1)
- added J13: Connector 16-bit, Connector_PinHeader_1.27mm:PinHeader_2x15_P1.27mm_Vertical_SMD, F.Cu at (83.8, 64.1)
- added J14: Connector A 8-bit, Connector_PinHeader_1.27mm:PinHeader_2x10_P1.27mm_Vertical_SMD, F.Cu at (102.2, 79.9)
- added J15: Connector B 8-bit, Connector_PinHeader_1.27mm:PinHeader_2x10_P1.27mm_Vertical_SMD, F.Cu at (102.2, 61.0)
- added J16: Connector A - 4 bit, Connector_PinHeader_1.27mm:PinHeader_2x08_P1.27mm_Vertical_SMD, F.Cu at (120.7, 78.7)
- added J17: Connector B - 4 bit, Connector_PinHeader_1.27mm:PinHeader_2x08_P1.27mm_Vertical_SMD, F.Cu at (120.5, 59.7)
- added J18: Connector A - 2 bit, Connector_PinHeader_1.27mm:PinHeader_2x05_P1.27mm_Vertical_SMD, F.Cu at (139.1, 76.8)
- added J19: Connector B - 2 bit, Connector_PinHeader_1.27mm:PinHeader_2x05_P1.27mm_Vertical_SMD, F.Cu at (139.1, 57.8)
- added J2: ~, Connector_USB:USB_A_Wuerth_61400826021_Horizontal_Stacked, F.Cu at (83.1, 135.0)
- added J3: ~, Connector_USB:USB_A_Wuerth_61400826021_Horizontal_Stacked, F.Cu at (62.9, 135.0)
- added J4: Micro_SD_Card, Connector_Card:microSD_HC_Wuerth_693072010801, F.Cu at (207.6, 139.6)
- added J5: I2C 2, Connector_PinHeader_2.54mm:PinHeader_2x03_P2.54mm_Vertical, F.Cu at (266.5, 61.3)
- added J6: Conn_01x03_Female, Connector_PinSocket_2.54mm:PinSocket_1x03_P2.54mm_Vertical, F.Cu at (58.8, 89.3)
- added J7: I2C 1, Connector_PinHeader_2.54mm:PinHeader_2x03_P2.54mm_Vertical, F.Cu at (273.7, 61.3)
- added J8: I2C 3, Connector_PinHeader_2.54mm:PinHeader_2x03_P2.54mm_Vertical, F.Cu at (280.9, 61.3)
- added J9: Conn_01x03_Female, Connector_PinHeader_2.54mm:PinHeader_1x03_P2.54mm_Vertical, F.Cu at (80.8, 105.7)
- added L1: 3.3u, footprints:NRS8030, F.Cu at (140.5, 99.3)
- added L2: 2.2u, footprints:IND_NR6028T4R7M, F.Cu at (123.6, 100.2)
- added R1: 1k, Resistor_SMD:R_0402_1005Metric_Pad0.72x0.64mm_HandSolder, F.Cu at (62.9, 56.1)
- added R10: 27.4R, Resistor_SMD:R_0402_1005Metric_Pad0.72x0.64mm_HandSolder, F.Cu at (62.3, 110.4)
- added R11: 27.4R, Resistor_SMD:R_0402_1005Metric_Pad0.72x0.64mm_HandSolder, F.Cu at (63.4, 110.4)
- added R12: 1k, Resistor_SMD:R_0402_1005Metric_Pad0.72x0.64mm_HandSolder, F.Cu at (299.2, 78.9)
- added R13: 10k, Resistor_SMD:R_0402_1005Metric_Pad0.72x0.64mm_HandSolder, F.Cu at (306.6, 60.0)
- added R14: 10k, Resistor_SMD:R_0402_1005Metric_Pad0.72x0.64mm_HandSolder, F.Cu at (306.6, 62.0)
- added R15: 1k, Resistor_SMD:R_0402_1005Metric_Pad0.72x0.64mm_HandSolder, F.Cu at (66.1, 92.5)
- added R16: 100k, Resistor_SMD:R_0402_1005Metric_Pad0.72x0.64mm_HandSolder, F.Cu at (252.4, 43.9)
- added R16: 10k, Resistor_SMD:R_0402_1005Metric_Pad0.72x0.64mm_HandSolder, F.Cu at (73.4, 105.9)
- added R17: 4.7, Resistor_SMD:R_0402_1005Metric_Pad0.72x0.64mm_HandSolder, F.Cu at (252.4, 45.9)
- added R17: 10k, Resistor_SMD:R_0402_1005Metric_Pad0.72x0.64mm_HandSolder, F.Cu at (76.8, 107.8)
- added R18: 10k, Resistor_SMD:R_0402_1005Metric_Pad0.72x0.64mm_HandSolder, F.Cu at (68.2, 81.4)
- added R2: 120k, Resistor_SMD:R_0402_1005Metric_Pad0.72x0.64mm_HandSolder, F.Cu at (138.4, 116.8)
- added R3: 3.3k, Resistor_SMD:R_0402_1005Metric_Pad0.72x0.64mm_HandSolder, F.Cu at (138.4, 115.7)
- added R4: 22k, Resistor_SMD:R_0402_1005Metric_Pad0.72x0.64mm_HandSolder, F.Cu at (138.4, 114.6)
- added R5: 68k, Resistor_SMD:R_0402_1005Metric_Pad0.72x0.64mm_HandSolder, F.Cu at (121.3, 116.9)
- added R6: 5.6k, Resistor_SMD:R_0402_1005Metric_Pad0.72x0.64mm_HandSolder, F.Cu at (121.3, 115.6)
- added R7: 22k, Resistor_SMD:R_0402_1005Metric_Pad0.72x0.64mm_HandSolder, F.Cu at (121.3, 114.4)
- added R8: 100k, Resistor_SMD:R_0402_1005Metric_Pad0.72x0.64mm_HandSolder, F.Cu at (43.2, 121.1)
- added R9: 4.7, Resistor_SMD:R_0402_1005Metric_Pad0.72x0.64mm_HandSolder, F.Cu at (43.2, 123.1)
- added S1: PTS636_SM43J_SMTR_LFS, footprints:SW_PTS636_SM43J_SMTR_LFS, F.Cu at (278.7, 104.6)
- added S2: PTS636_SM43J_SMTR_LFS, footprints:SW_PTS636_SM43J_SMTR_LFS, F.Cu at (299.1, 96.3)
- added TP1: TestPoint, TestPoint:TestPoint_Loop_D1.80mm_Drill1.0mm_Beaded, F.Cu at (245.9, 88.2)
- added TP2: TestPoint, TestPoint:TestPoint_Pad_D1.5mm, F.Cu at (260.4, 83.8)
- added TP3: TestPoint, TestPoint:TestPoint_Pad_D1.0mm, F.Cu at (249.8, 87.4)
- added TP4: TestPoint, TestPoint:TestPoint_Pad_D1.0mm, F.Cu at (249.8, 90.5)
- added TP5: TestPoint, TestPoint:TestPoint_Pad_D1.5mm, F.Cu at (143.0, 87.8)
- added TP6: TestPoint, TestPoint:TestPoint_Pad_D1.5mm, F.Cu at (126.0, 89.3)
- added U1: RP2040, footprints:QFN40P700X700X90-57N, F.Cu at (61.7, 64.8)
- added U10: GD25D05CT, Package_SO:SOP-8_3.9x4.9mm_P1.27mm, F.Cu at (73.3, 110.4)
- added U11: W25Q128JVS, Package_SO:SOIC-8_5.23x5.23mm_P1.27mm, F.Cu at (64.6, 78.0)
- added U2: LD1117S50TR_SOT223, Package_TO_SOT_SMD:SOT-223-3_TabPin2, F.Cu at (115.4, 146.4)
- added U3: AP2210, Package_TO_SOT_SMD:SOT-23-5_HandSoldering, F.Cu at (249.4, 79.6)
- added U4: AP2210, Package_TO_SOT_SMD:SOT-23-5_HandSoldering, F.Cu at (167.4, 127.6)
- added U5: BD9D321EFJ, footprints:SOIC127P600X100-9N, F.Cu at (140.1, 109.9)
- added U6: BD9D321EFJ, footprints:SOIC127P600X100-9N, F.Cu at (122.9, 109.7)
- added U7: hs8836a, Package_SO:SOP-16_3.9x9.9mm_P1.27mm, F.Cu at (75.7, 124.0)
- added U8: RP2040, footprints:QFN40P700X700X90-57N, F.Cu at (64.0, 101.2)
- added U9: TLV320DAC3203IRGET, Package_DFN_QFN:VQFN-24-1EP_4x4mm_P0.5mm_EP2.45x2.45mm_ThermalVias, F.Cu at (244.0, 97.8)
- added Y1: ECS-120-8-36-CGN-TR, footprints:XTAL_ECS-120-8-36-CGN-TR, F.Cu at (65.1, 55.2)
- added Y2: ECS-120-8-36-CGN-TR, footprints:XTAL_ECS-120-8-36-CGN-TR, F.Cu at (68.2, 92.9)
- C203, C205: footprint Capacitor_SMD:C_0603_1608Metric_Pad1.08x0.95mm_HandSolder -> Capacitor_SMD:C_0402_1005Metric_Pad0.74x0.62mm_HandSolder
- C207: footprint Capacitor_SMD:C_0603_1608Metric_Pad1.08x0.95mm_HandSolder -> Capacitor_SMD:C_0402_1005Metric_Pad0.74x0.62mm_HandSolder; moved to F.Cu
- moved C205 156.0 mm to (196.4, 113.3), turned to 0 degrees
- moved C203 155.9 mm to (196.4, 111.3), turned to 0 degrees
- moved C207 151.8 mm to (196.4, 115.3), turned to 0 degrees
- moved J1 23.9 mm to (137.0, 126.1), turned to 0 degrees
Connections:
- net +3V3 renamed +3V3_MCU
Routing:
- net +3V3_MCU: track 537.6 -> 72.9 mm, vias 5 -> 12
- net VDC: track 393.8 -> 75.8 mm, vias 4 -> 0
- net +5V_BUS: track 345.1 -> 146.3 mm, vias 2 -> 3
- net /Connectors/BUS.RWDS: track 176.8 -> 0.00 mm
- net /Connectors/BUS.D1: track 176.4 -> 0.00 mm
- net /Connectors/BUS.D0: track 176.2 -> 0.00 mm
- net /Connectors/BUS.SCLK: track 175.8 -> 0.00 mm
- net /Connectors/BUS.D3: track 144.3 -> 0.00 mm
- net /Connectors/BUS.D2: track 143.3 -> 0.00 mm
- net /Connectors/BUS.D6: track 110.8 -> 0.00 mm
- net /Connectors/BUS.D4: track 110.8 -> 0.00 mm
- net /Connectors/BUS.D7: track 110.7 -> 0.00 mm
- net /Connectors/BUS.D5: track 110.7 -> 0.00 mm
- net /Bus multiplexers & demultiplexers/BUS_INT6: track 109.4 -> 0.00 mm
- net /Connectors/I2C.SDA: track 102.9 -> 0.00 mm
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- added copper zone on In1.Cu, net GND
- added copper zone on In2.Cu, net GND
- removed copper zone on B.Cu, net GND
- removed copper zone on F.Cu, net GND
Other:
- board size 100 x 100 mm -> 99.2 x 94.1 mm
- copper layers 2 -> 4
